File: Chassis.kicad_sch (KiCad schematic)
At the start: 48 parts, among them J1 FR_JST, J10 IN_XT30, J11 SWD_IN, J12 Conn_01x08_Pin, J13 GIM1_JST, J14 GIM2_JST, J15 GIM1_XT30, J16 GIM2_XT30, J17 SWD_OUT, J18 CHA_XT30, J19 SHOO_XT30, J2 BR_JST, J20 GIM_XT30, J21 OUT_JST, J22 5V_XT30, J23 UART_IN, J24 UART_Out, J25 REF_IN, J26 REF_OUT, J27 CAN2_IN, J28 CAN2_OUT, J3 FL_JST, J4 BL_JST, J5 FR_XT30, J6 BR_XT30, J7 FL_XT30, J8 BL_XT30, J9 IN_JST

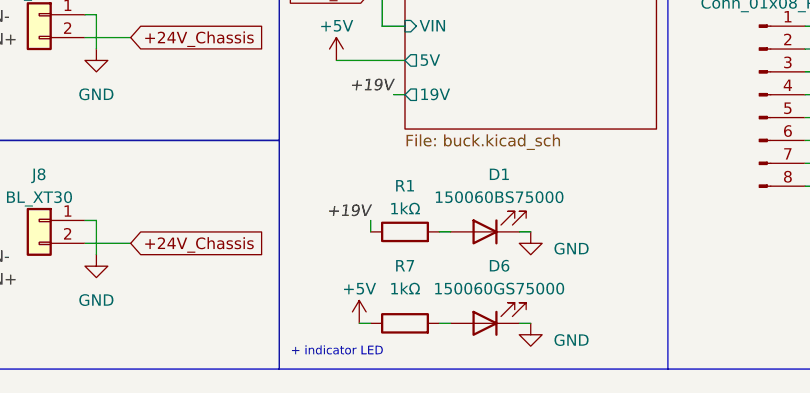
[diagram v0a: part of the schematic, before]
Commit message: Change output filtering for the +19V to 0805 (Mouser doesn't have 0603)
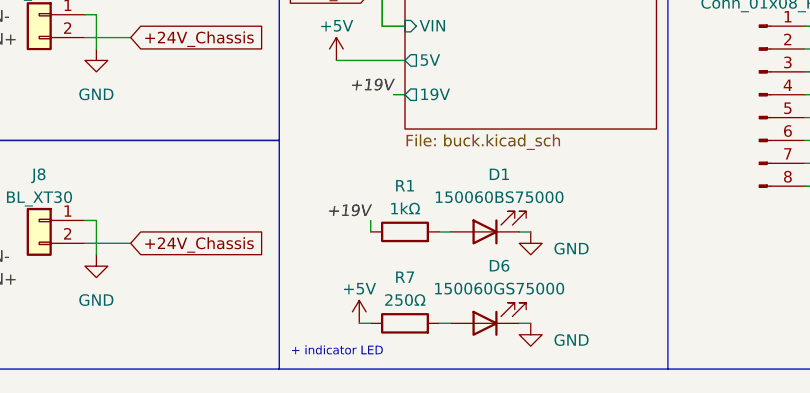
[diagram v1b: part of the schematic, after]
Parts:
- D1: Mouser Part Number 710-150060BS75000 -> (none)
- F1: Mouser Part Number 530-0ABB-2500-TM -> (none)
- R1, R10, R2, R8, R9: Mouser Part Number 603-RE0603FRE071KL -> (none)
- R7: value 1kΩ -> 250Ω; Mouser Part Number 603-RE0603FRE071KL -> (none)
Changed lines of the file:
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@@
-      (effects (font (size 1.27 1.27)) hide)
-    )
-    (property "Mouser Part Number" "530-0ABB-2500-TM" (at 68.58 39.37 0)
       (effects (font (size 1.27 1.27)) hide)
     )
@@
       (effects (font (size 1.27 1.27)) hide)
     )
-    (property "Mouser Part Number" "603-RE0603FRE071KL" (at 184.15 97.79 0)
-      (effects (font (size 1.27 1.27)) hide)
-    )
     (pin "1")
     (pin "2")
@@
     )
     (property "Datasheet" "~" (at 135.89 97.79 0)
-      (effects (font (size 1.27 1.27)) hide)
-    )
-    (property "Mouser Part Number" "603-RE0603FRE071KL" (at 140.97 97.79 0)
       (effects (font (size 1.27 1.27)) hide)
     )
@@
   (symbol (lib_id "Device:R") (at 99.06 158.75 90) (unit 1)
     (in_bom yes) (on_board yes) (dnp no) (fields_autoplaced)
-    (property "Reference" "R7" (at 99.06 152.4 90)
-      (effects (font (size 1.27 1.27)))
-    )
-    (property "Value" "1kΩ" (at 99.06 154.94 90)
+    (property "Reference" "R7" (at 99.06 153.67 90)
+      (effects (font (size 1.27 1.27)))
+    )
+    (property "Value" "250Ω" (at 99.06 156.21 90)
       (effects (font (size 1.27 1.27)))
     )
@@
     )
     (property "Datasheet" "~" (at 99.06 158.75 0)
-      (effects (font (size 1.27 1.27)) hide)
-    )
-    (property "Mouser Part Number" "603-RE0603FRE071KL" (at 99.06 158.75 0)
       (effects (font (size 1.27 1.27)) hide)
     )
@@
       (effects (font (size 1.27 1.27)) hide)
     )
-    (property "Mouser Part Number" "603-RE0603FRE071KL" (at 163.83 97.79 0)
-      (effects (font (size 1.27 1.27)) hide)
-    )
     (pin "1")
     (pin "2")
@@
       (effects (font (size 1.27 1.27)) hide)
     )
-    (property "Mouser Part Number" "603-RE0603FRE071KL" (at 119.38 97.79 0)
-      (effects (font (size 1.27 1.27)) hide)
-    )
     (pin "1")
     (pin "2")
@@
       (effects (font (size 1.27 1.27)) hide)
     )
-    (property "Mouser Part Number" "710-150060BS75000" (at 107.95 148.59 0)
-      (effects (font (size 1.27 1.27)) hide)
-    )
     (pin "1")
     (pin "2")
@@
       (effects (font (size 1.27 1.27)) hide)
     )
-    (property "Mouser Part Number" "603-RE0603FRE071KL" (at 99.06 148.59 0)
-      (effects (font (size 1.27 1.27)) hide)
-    )

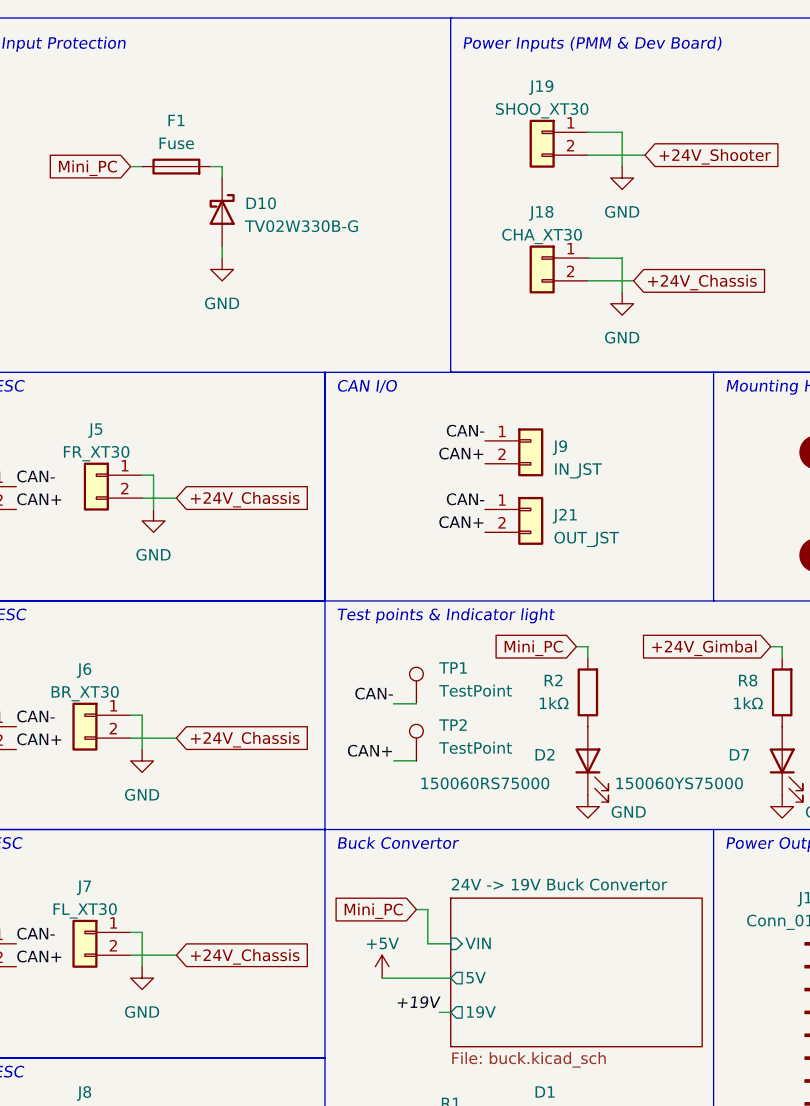
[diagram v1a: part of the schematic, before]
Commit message: Fix power protection + adj silk
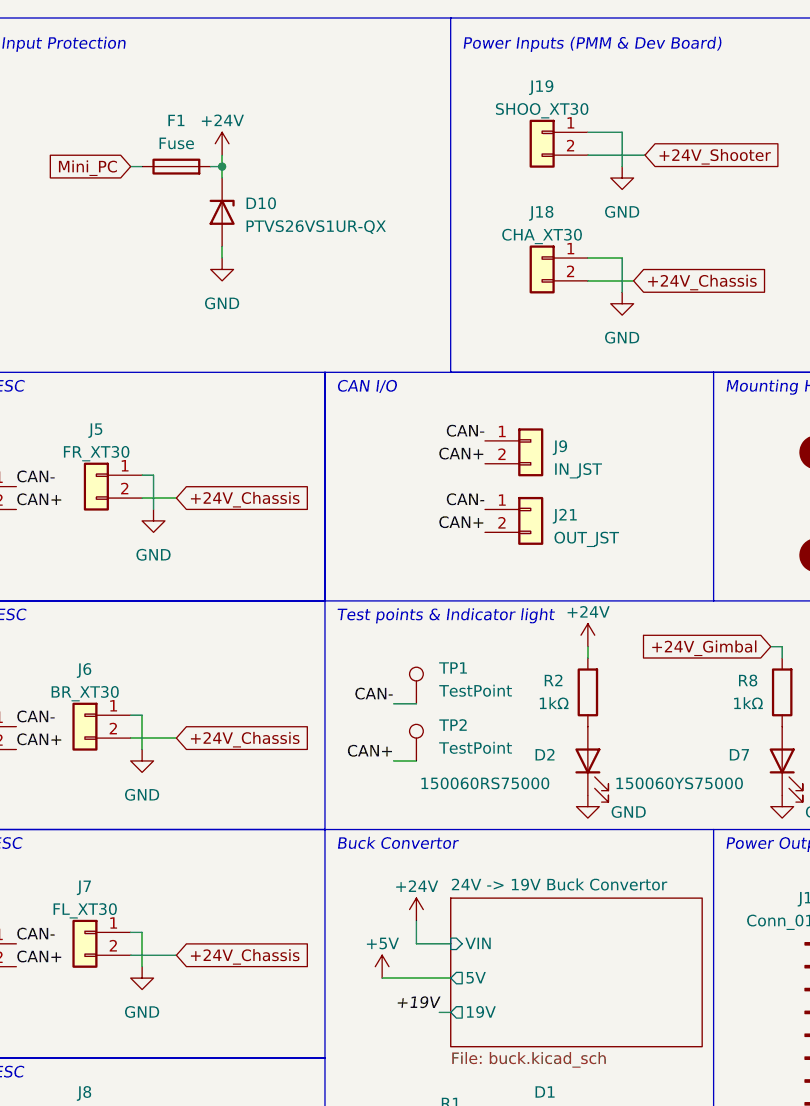
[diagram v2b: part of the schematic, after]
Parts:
- D10: value TV02W330B-G -> PTVS26VS1UR-QX; footprint Diode_SMD:D_SOD-123 -> Robomaster_Passives:PTVS26VS1URQX; symbol Device:D_Schottky -> Device:D_Zener
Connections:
- net Mini_PC: no longer R2.2
- net +24V: now reaches D10.1 (K), F1.2
- net +24V: now also R2.2

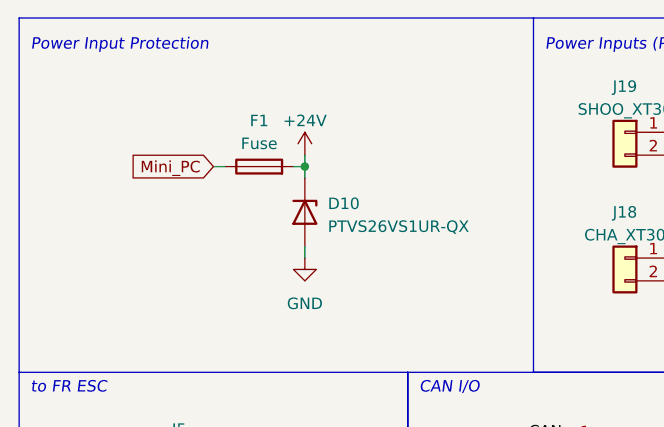
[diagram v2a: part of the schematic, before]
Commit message: Update and generate IBOM
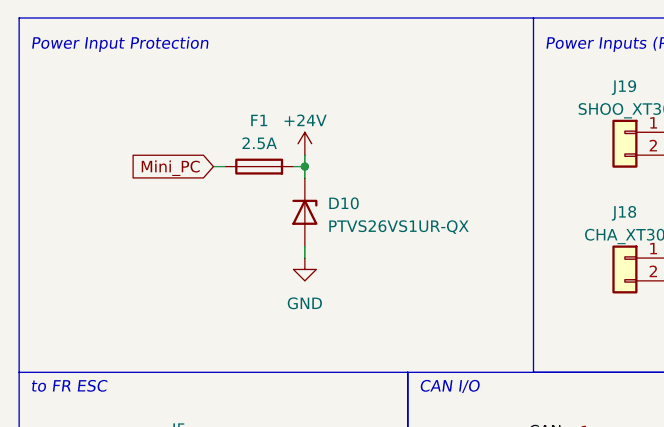
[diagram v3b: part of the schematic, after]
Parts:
- D1: Manufacturer_Part_Number (none) -> 150060BS75000; Mouser Part Number (none) -> 710-150060BS75000
- D10: Manufacturer_Part_Number (none) -> PTVS26VS1UR-QX; Mouser Part Number (none) -> 771-PTVS26VS1UR-QX
- D2: Manufacturer_Part_Number (none) -> 150060RS75000; Mouser Part Number (none) -> 710-150060RS75000
- D6: Manufacturer_Part_Number (none) -> 150060GS75000; Mouser Part Number (none) -> 710-150060GS75000
- D7, D8, D9: Manufacturer_Part_Number (none) -> 150060YS75000; Mouser Part Number (none) -> 710-150060YS75000
- F1: value Fuse -> 2.5A; Manufacturer_Part_Number (none) -> ERB-RE2R50V; Mouser Part Number (none) -> 667-ERB-RE2R50V
- J1, J13, J14, J2, J21, J27, J28, J3, J4, J9: Manufacturer_Part_Number (none) -> JST 2-pin
- J10, J15, J16, J18, J19, J20, J22, J5, J6, J7, J8: Manufacturer_Part_Number (none) -> XT30
- J11, J17, J23, J24, J25, J26: Manufacturer_Part_Number (none) -> JST 4-pin
- J12: Manufacturer_Part_Number (none) -> 172298-1108; Mouser Part Number (none) -> 538-172298-1108
- R1, R10, R2, R8, R9: Manufacturer_Part_Number (none) -> RT0603DRD071KL; Mouser Part Number (none) -> 603-RT0603DRD071KL
- R7: Manufacturer_Part_Number (none) -> MCT06030E2500BP100; Mouser Part Number (none) -> 594-MCT06030E2500BP1

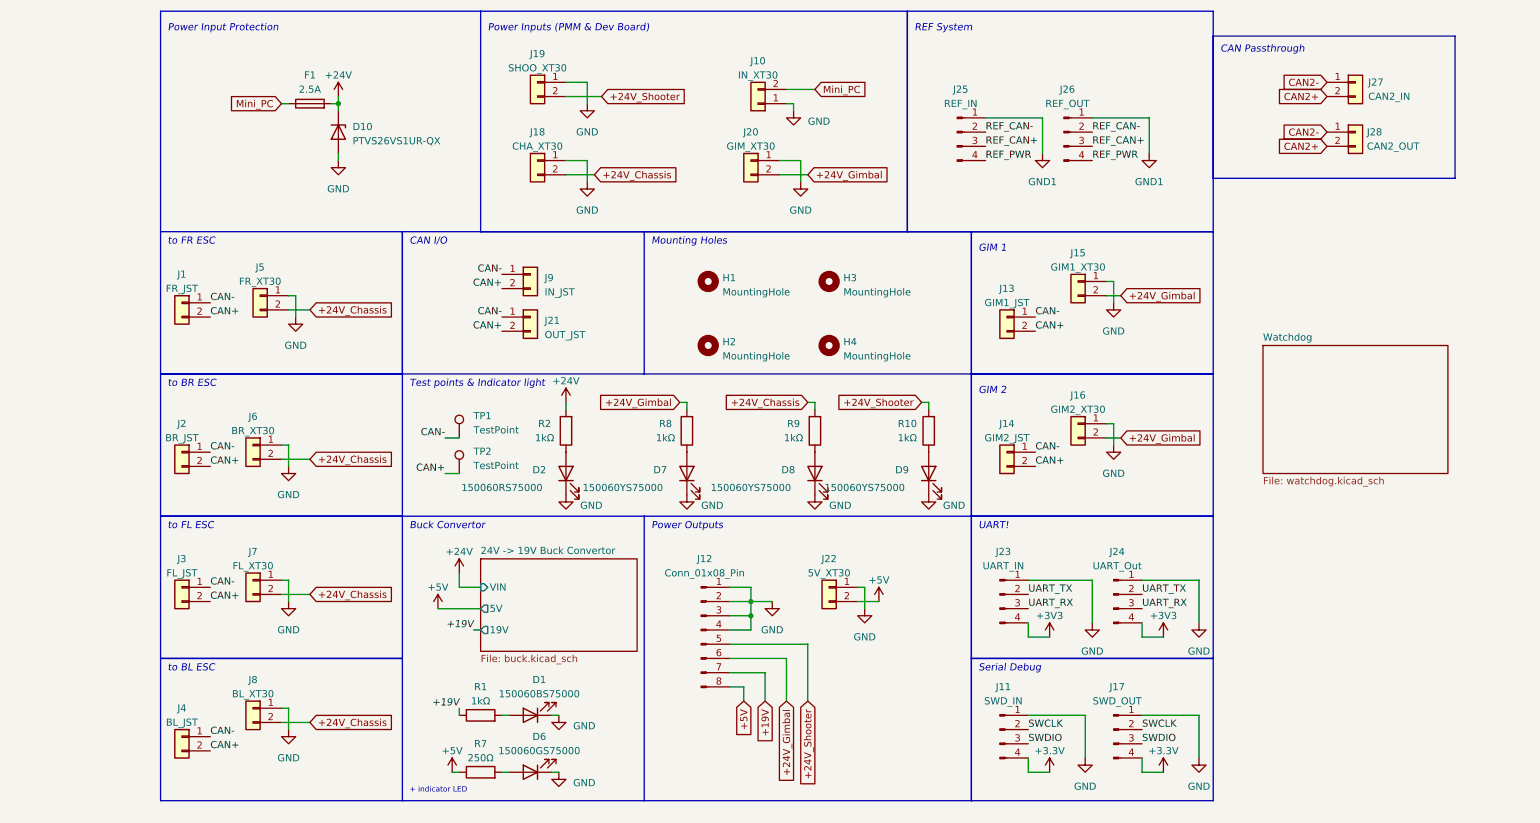
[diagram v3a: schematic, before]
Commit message: Andrew added hierarchical labels to in/out pins on schematic
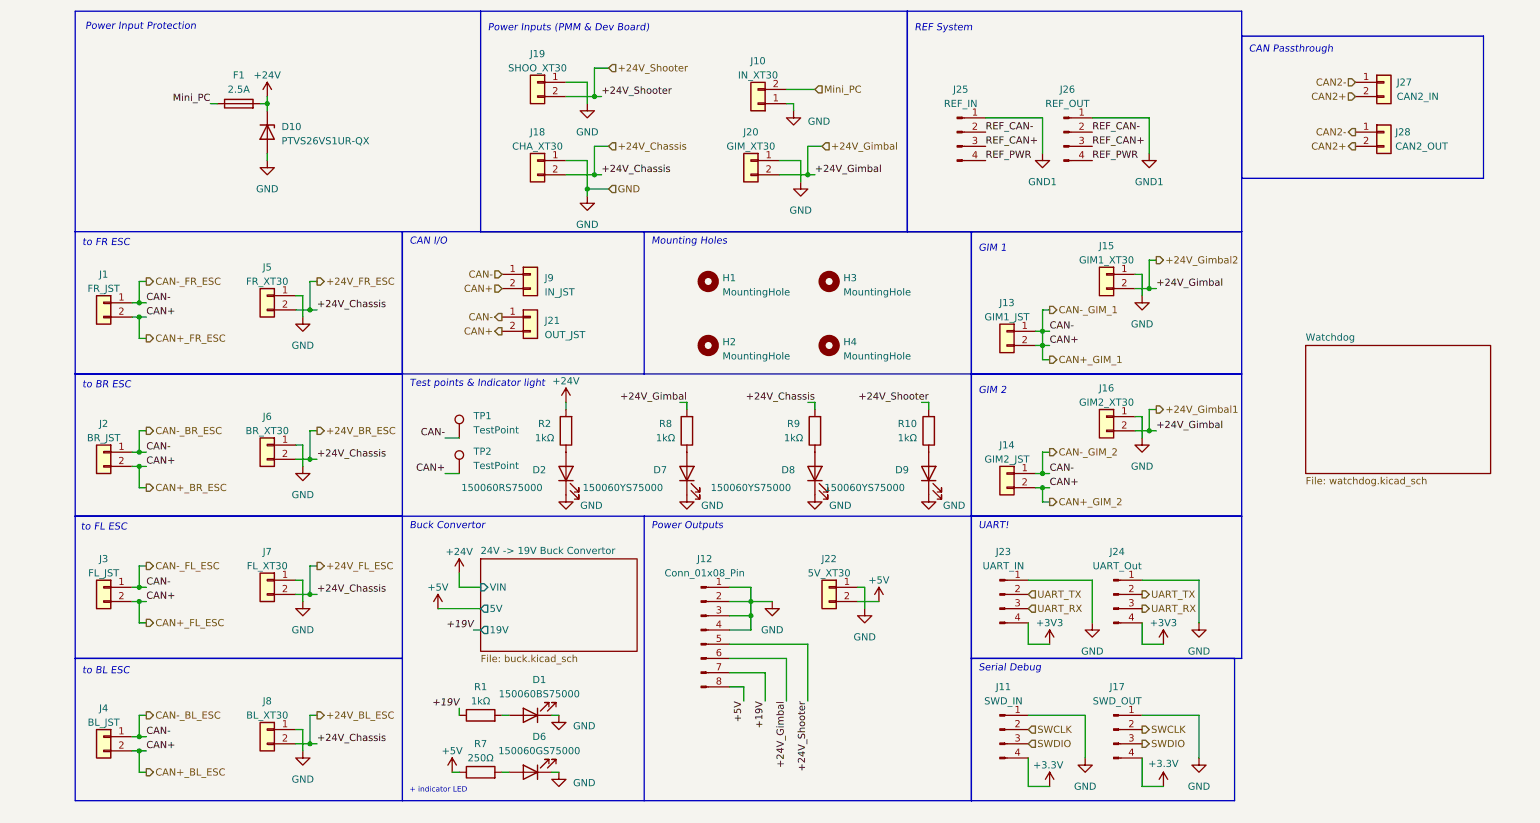
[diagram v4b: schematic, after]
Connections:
- net CAN- is gone; now on net CAN+: J1.1 (Pin_1), J13.1 (Pin_1), J14.1 (Pin_1), J2.1 (Pin_1), J21.1 (Pin_1), J3.1 (Pin_1), J4.1 (Pin_1), J9.1 (Pin_1), TP1.1
- net +24V_Chassis renamed +24V_BL_ESC
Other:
- moved on the sheet: D10, F1, J1, J13, J14, J15, J16, J2, J27, J28, J3, J4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

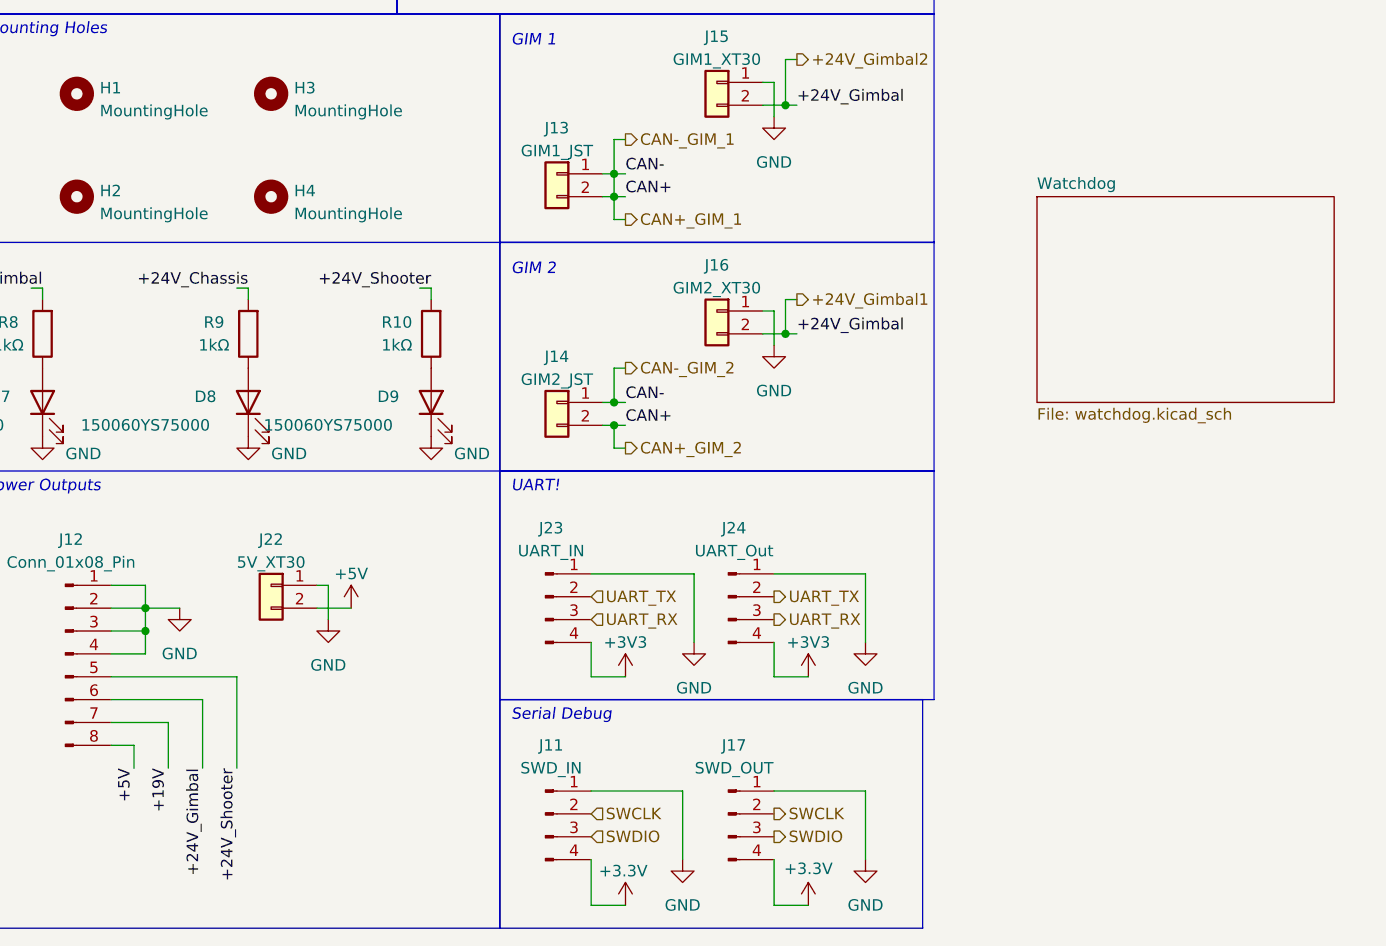
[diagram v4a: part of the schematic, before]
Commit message: added i2c and chassis power to supercap to schematic
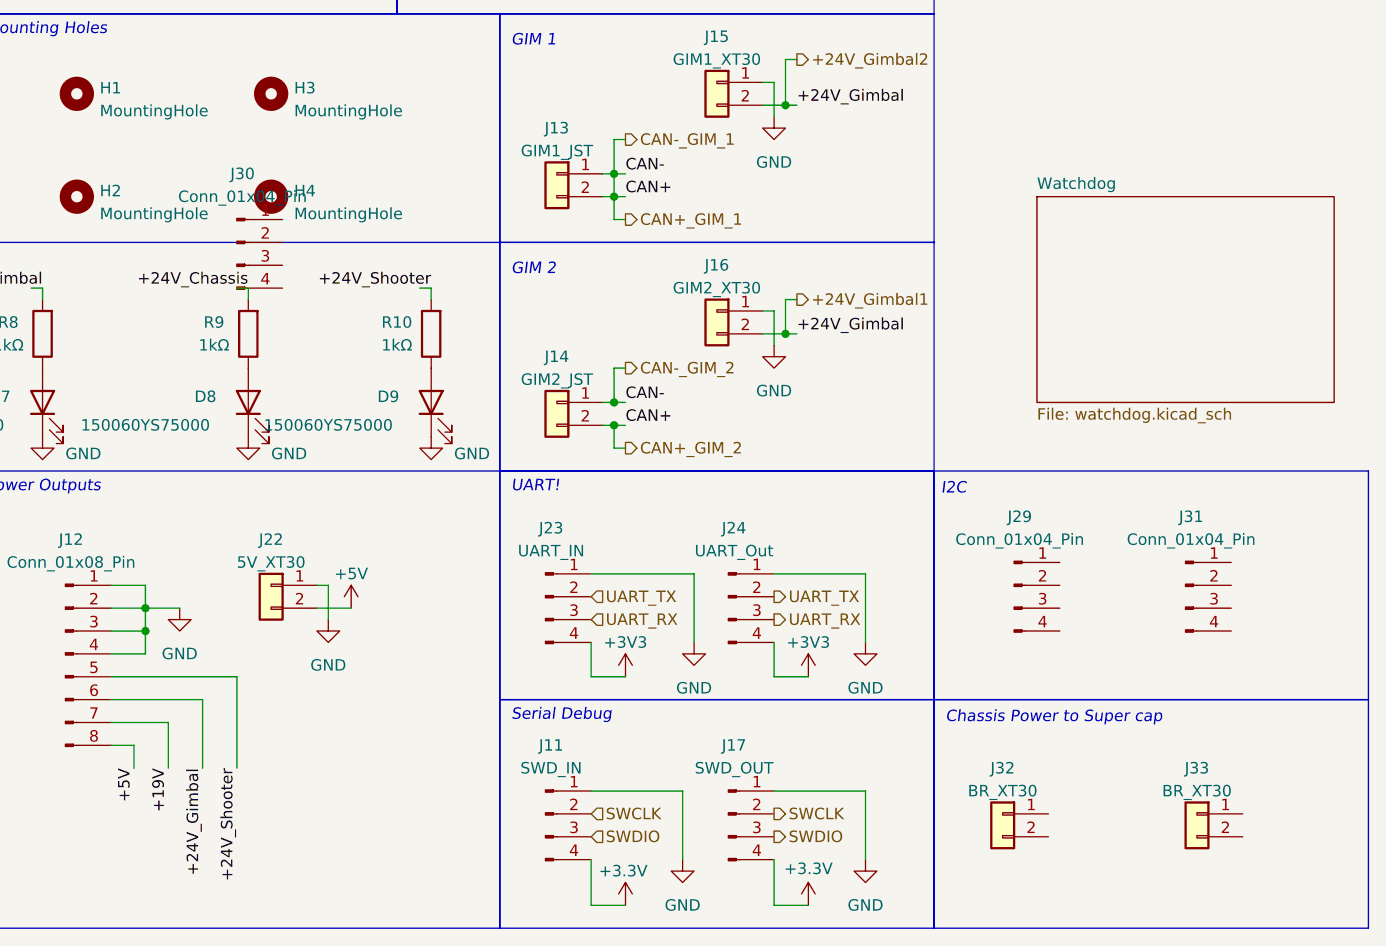
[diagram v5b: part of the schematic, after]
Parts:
- added J29, J30, J31: Conn_01x04_Pin, symbol Connector:Conn_01x04_Pin
- added J32, J33: BR_XT30, Robomaster_Connectors:AMASS_XT30U-F_1x02_P5.0mm_Vertical, symbol Connector_Generic:Conn_01x02
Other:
- note added: "Chassis Power to Super cap"
- note added: "I2C"
